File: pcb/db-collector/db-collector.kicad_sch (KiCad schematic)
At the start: 18 parts, among them IC1 ICS-43432, IC2 TLV75533PDYDR, J1 Power, U1 XAIO ESP32-C3

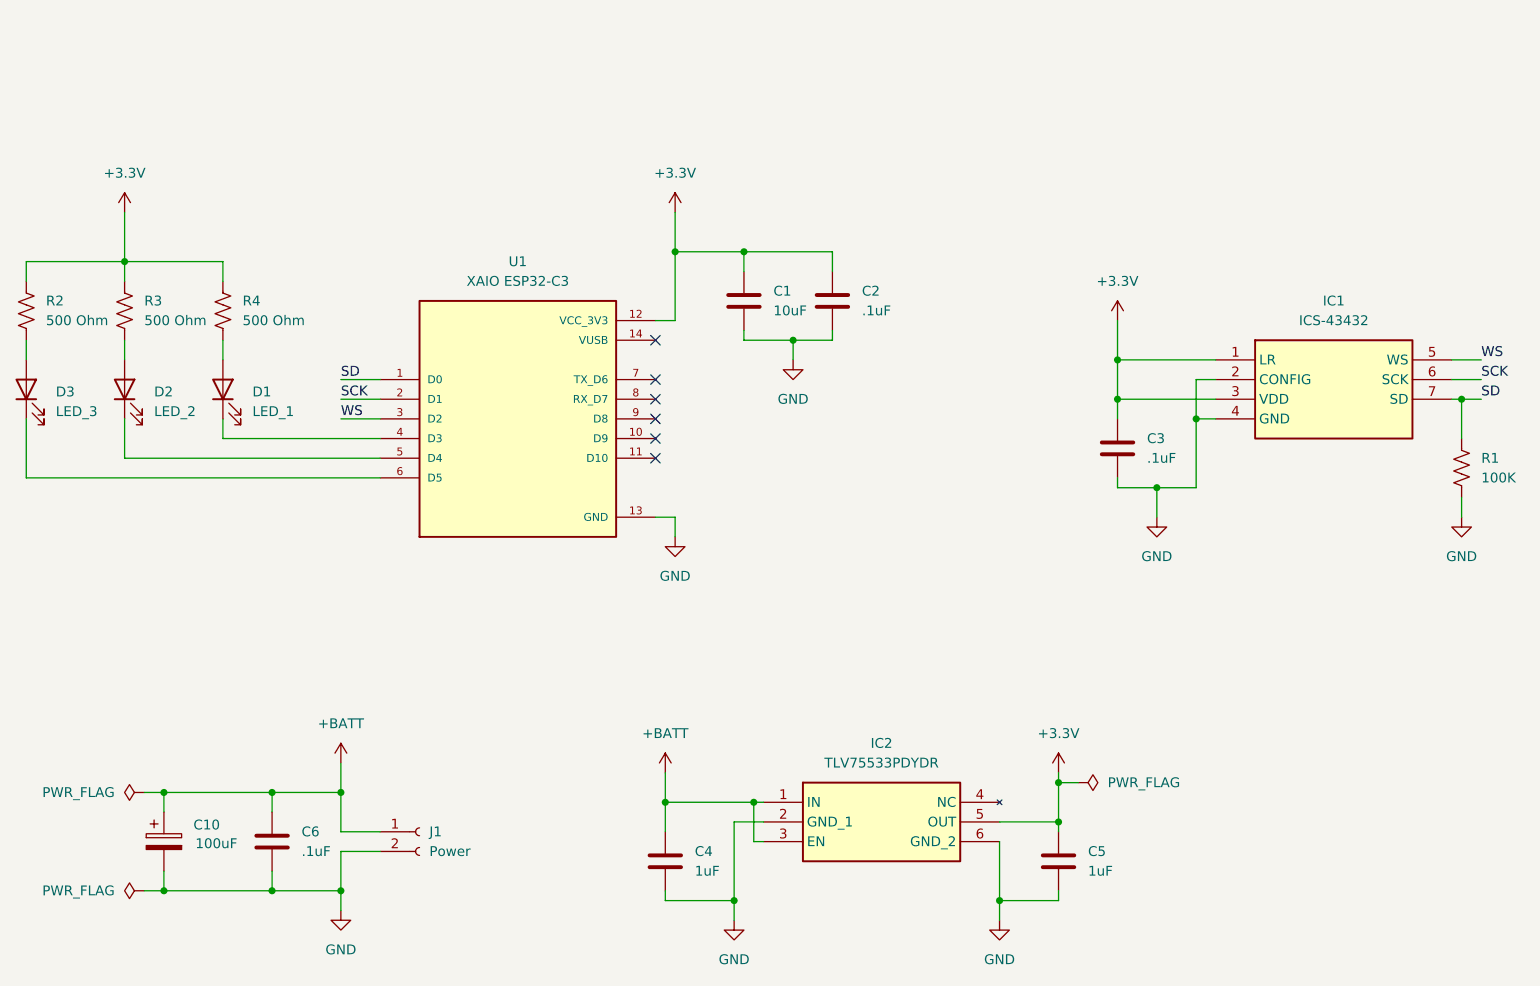
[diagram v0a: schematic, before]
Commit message: New simplified db-collector.  Big change is that the battery attaches directly to the ESP32-c3 XIAO battery terminals and lets it do the voltage regulation.  This gets around how finicky the ESP is to slow voltage rampup on the 3V3 rail.
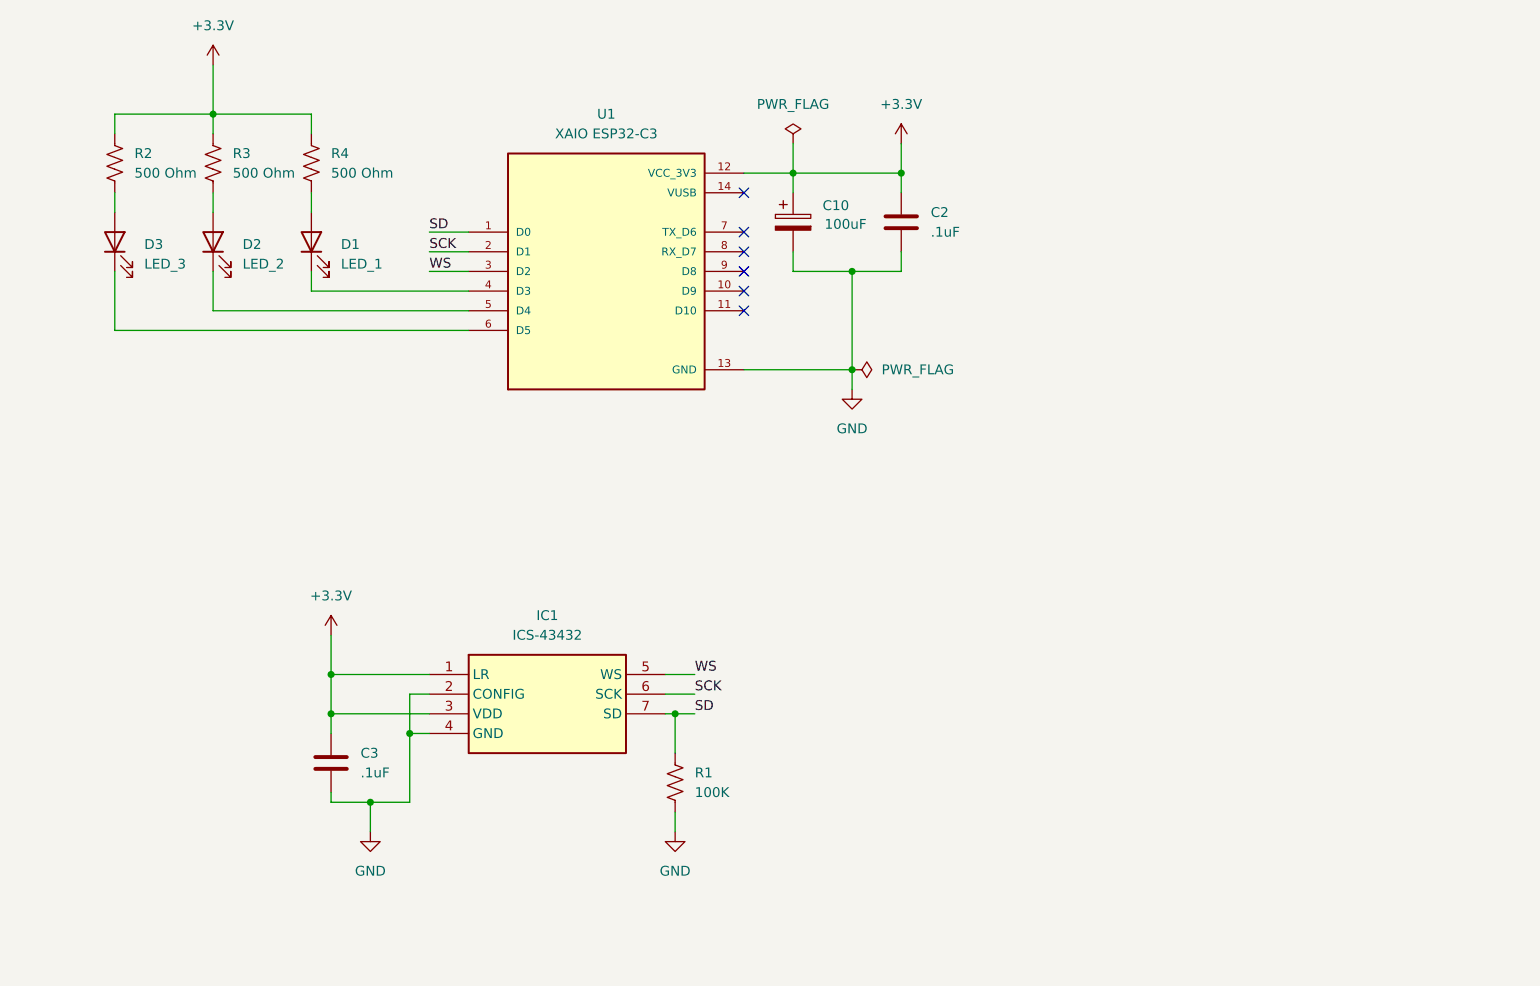
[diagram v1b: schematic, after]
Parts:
- removed C1: 10uF, Capacitor_SMD:C_0805_2012Metric_Pad1.18x1.45mm_HandSolder, symbol Device:C
- removed C4, C5: 1uF, Capacitor_SMD:C_0805_2012Metric_Pad1.18x1.45mm_HandSolder, symbol Device:C
- removed C6: .1uF, Capacitor_SMD:C_0805_2012Metric_Pad1.18x1.45mm_HandSolder, symbol Device:C
- removed IC2: TLV75533PDYDR, Garth:TLV75533PDYDR, symbol Garth Libraries:TLV75533PDYDR
- removed J1: Power, Connector_PinHeader_2.54mm:PinHeader_1x02_P2.54mm_Vertical, symbol Connector:Conn_01x02_Socket
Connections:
- net +BATT is gone; now on net +3.3V: C10.1
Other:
- moved on the sheet: C10, C2, C3, D1, D2, D3, IC1, R1, R2, R3, R4, U1
